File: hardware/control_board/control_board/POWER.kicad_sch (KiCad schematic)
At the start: 94 parts, among them J4 Barrel_Jack_Switch, U10 TPS54360DDA, U11 TPS62933, U12 TPS54360DDA, U13 TPS54360DDA, U9 TPS54360DDA

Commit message: debug：蜂鸣器驱动电路；debug LED；电源输出排针
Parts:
- TP11: value +1V -> +3.3V
- renumbered C126 to C14, C186 to C15, C188 to C16, C190 to C17, C125 to C18, C130 to C19, C132 to C20, C161 to C21, C191 to C22, C122 to C23, C179 to C24, C182 to C25, C183 to C26, C121 to C27, C128 to C28, C131 to C29, C144 to C30, C184 to C31, C127 to C32, C129 to C33, C123 to C34, C124 to C35, C156 to C36, C185 to C37, C187 to C38, C189 to C39, C150 to C40, C151 to C41, C159 to C42, C160 to C43, C162 to C44, C163 to C45, C136 to C46, C178 to C47, C180 to C48, C181 to C49, C135 to C50, C143 to C51, C139 to C52, C142 to C53, C140 to C54, C141 to C55, C157 to C56, C158 to C57, C137 to C58, C138 to C59, C149 to C60, C145 to C61, C146 to C62, C147 to C63, C152 to C64, C153 to C65, C154 to C66, C155 to C67, C148 to C68, D8 to D4, D6 to D5, D4 to D6, D5 to D8, L16 to L1, L13 to L2, L17 to L3, L14 to L4, L15 to L5, R69 to R12, R75 to R13, R76 to R14, R73 to R15, R62 to R16, R63 to R17, R64 to R18, R61 to R19, R72 to R20, R77 to R21, R78 to R22, R74 to R23, R65 to R24, R67 to R25, R68 to R26, R66 to R27, R70 to R28, R71 to R29, TP12 to TP7, TP9 to TP8, TP13 to TP9, U12 to U3, U9 to U4, U13 to U5, U10 to U6, U11 to U7
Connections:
- net +1V0 renamed +3.3V
- no-connect marks 0 -> 1

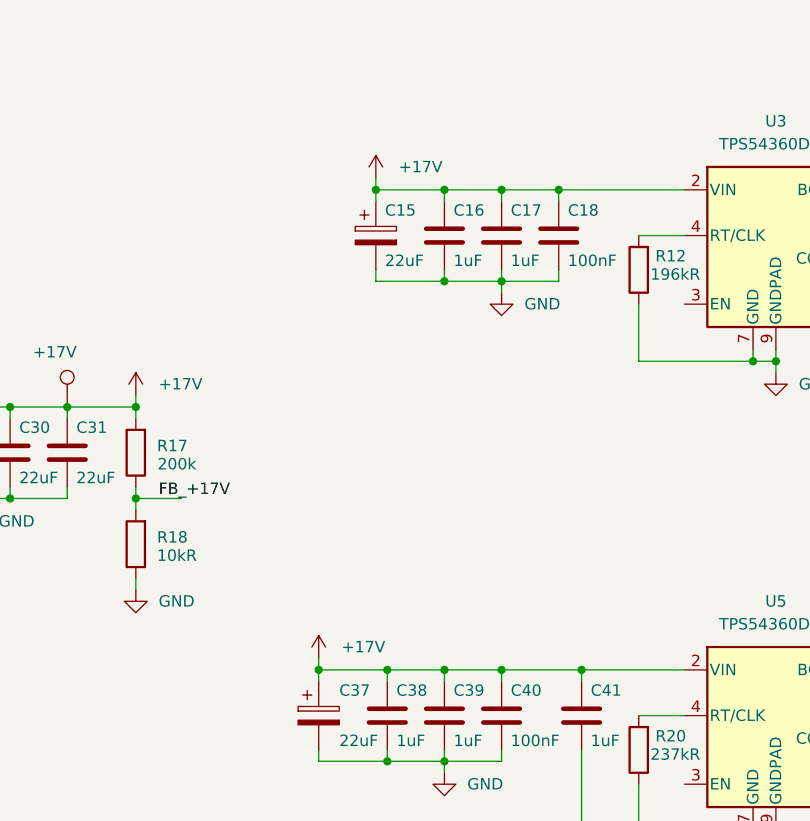
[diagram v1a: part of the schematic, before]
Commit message: feat：根据PCB微调原理图
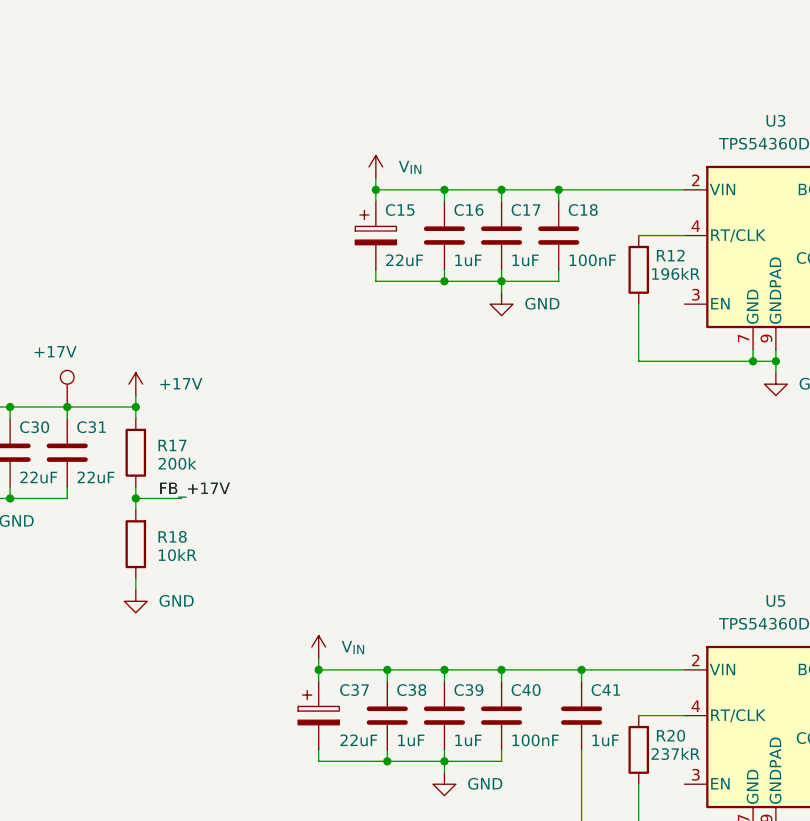
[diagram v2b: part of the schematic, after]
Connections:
- net +17V: no longer C15.1, C16.2, C17.2, C18.2, C37.1, C38.2, C39.2, C40.2, C41.2, U3.2 (VIN), U5.2 (VIN)
- net V_{IN}: now also C15.1, C16.2, C17.2, C18.2, C37.1, C38.2, C39.2, C40.2, C41.2, U3.2 (VIN), U5.2 (VIN)
